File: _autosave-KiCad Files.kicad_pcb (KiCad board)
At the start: 2 copper layers, 24 parts, among them SW1 SW_Push, U1 ATmega32U4-A, Y1 16MHz

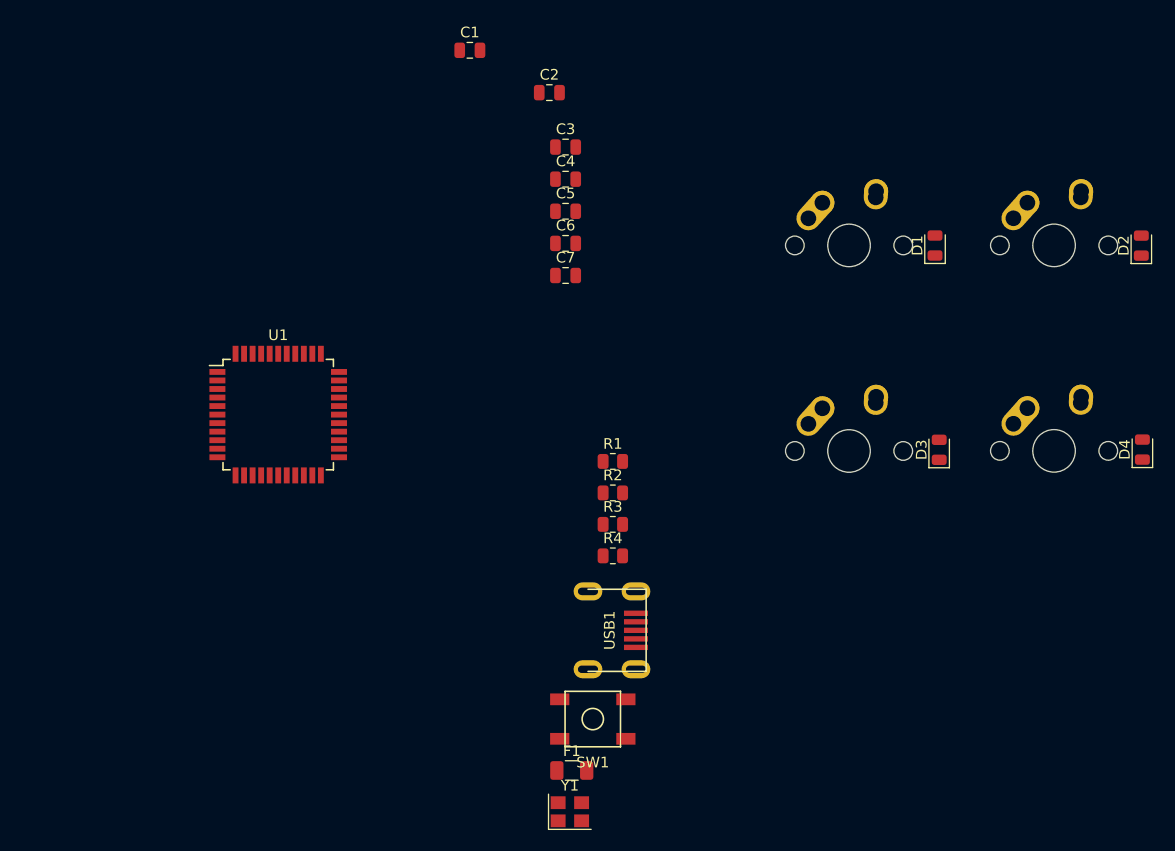
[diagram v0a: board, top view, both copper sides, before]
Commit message: PCB Outline.
Outlined the PCB, with organized components, rounded edges, and beginning to trace
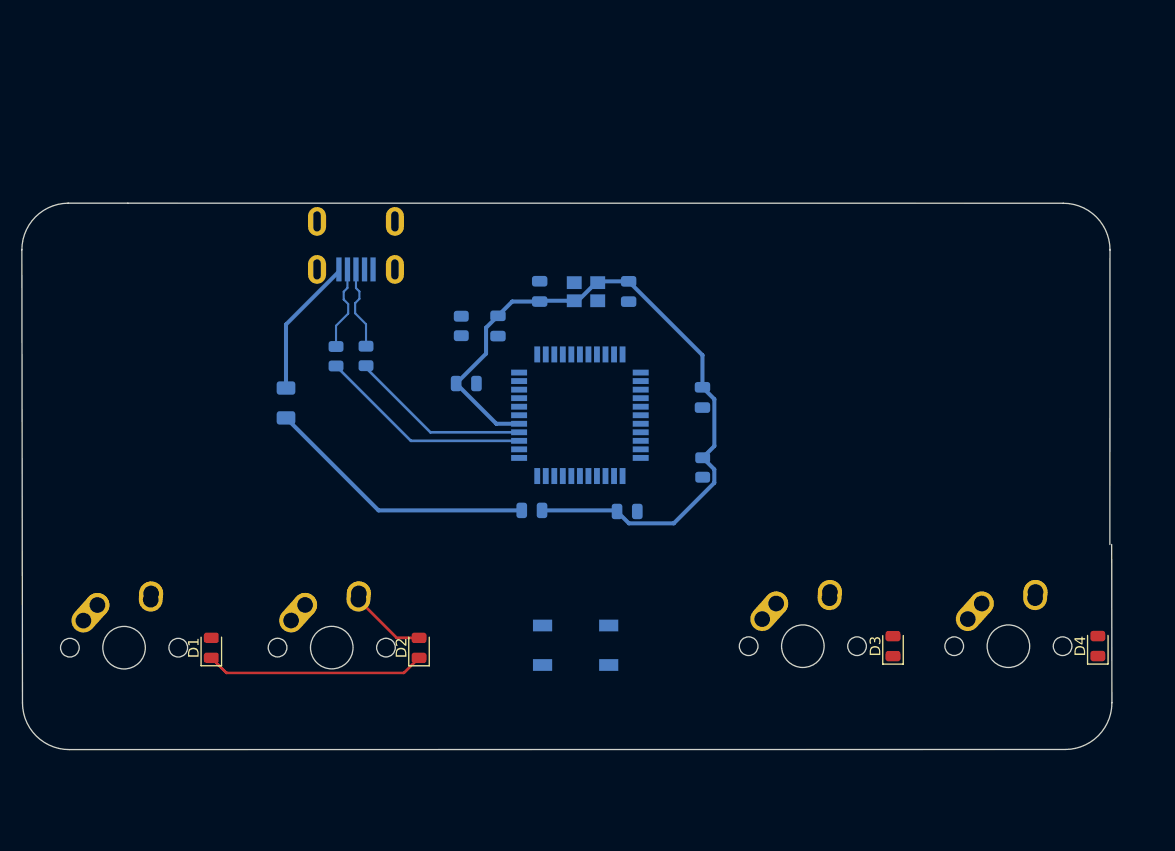
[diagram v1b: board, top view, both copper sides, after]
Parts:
- C1, C2, C3, C4, C5, C6, C7, F1, R1, R2, R3, R4, SW1, U1, USB1, Y1: moved to B.Cu
- moved MX1 77.7 mm to (100.8, 113.2)
- moved D1 77.6 mm to (109.0, 113.2)
- moved MX2 77.5 mm to (120.2, 113.1)
- moved D2 77.5 mm to (128.4, 113.2)
- moved Y1 48.8 mm to (144.1, 79.8), turned to 180 degrees
- moved USB1 44.1 mm to (122.5, 73.2), turned to -90 degrees
- moved F1 43.6 mm to (116.0, 90.2), turned to -90 degrees
- moved R3 30.4 mm to (120.7, 85.8), turned to -90 degrees
- moved U1 28.3 mm to (143.5, 91.4)
- moved C1 27.1 mm to (148.1, 79.8), turned to -90 degrees
- moved R2 26.5 mm to (123.5, 85.8), turned to -90 degrees
- moved C6 25.8 mm to (147.9, 100.4), turned to 180 degrees
- moved C3 24.0 mm to (132.9, 88.4), turned to 180 degrees
- moved C7 22.2 mm to (139.0, 100.3)
- moved C5 21.7 mm to (155.0, 89.7), turned to 90 degrees
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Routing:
- net GND: track 0.00 -> 70.4 mm
- net +5V: track 0.00 -> 25.7 mm
- net ROW0: track 0.00 -> 20.6 mm
- net Net-(U1-D-): track 0.00 -> 20.1 mm
- net Net-(U1-D+): track 0.00 -> 17.4 mm
- net VCC: track 0.00 -> 13.2 mm
- net D-: track 0.00 -> 8.02 mm
- net D+: track 0.00 -> 7.92 mm
- net Net-(D2-A): track 0.00 -> 7.16 mm
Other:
- board outline added: 102.2 x 51.2 mm
